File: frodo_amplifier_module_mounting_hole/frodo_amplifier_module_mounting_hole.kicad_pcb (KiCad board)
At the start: 2 copper layers, 16.5 x 24 mm, 24 parts, among them IC1 INA826AID, IC2 AS321KTR-G1, J1 Conn_01x01_Socket, J2 Conn_01x01_Socket, J3 Conn_01x01_Socket, J4 Conn_01x01_Socket, J5 Conn_01x01_Socket, J6 Conn_01x01_Socket, J7 Conn_01x01_Socket, J8 Conn_01x01_Socket

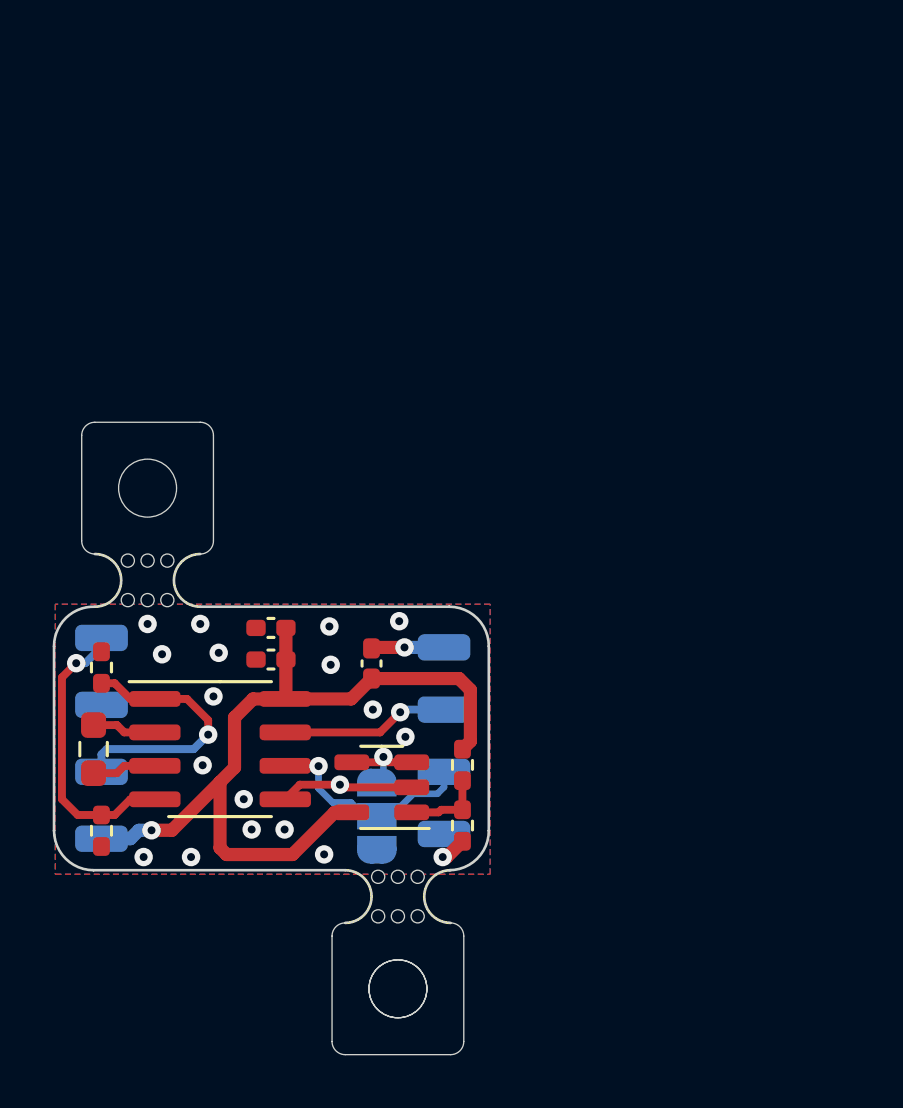
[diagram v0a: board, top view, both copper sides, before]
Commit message: updated mounting holes and footprints of c2 and fb1
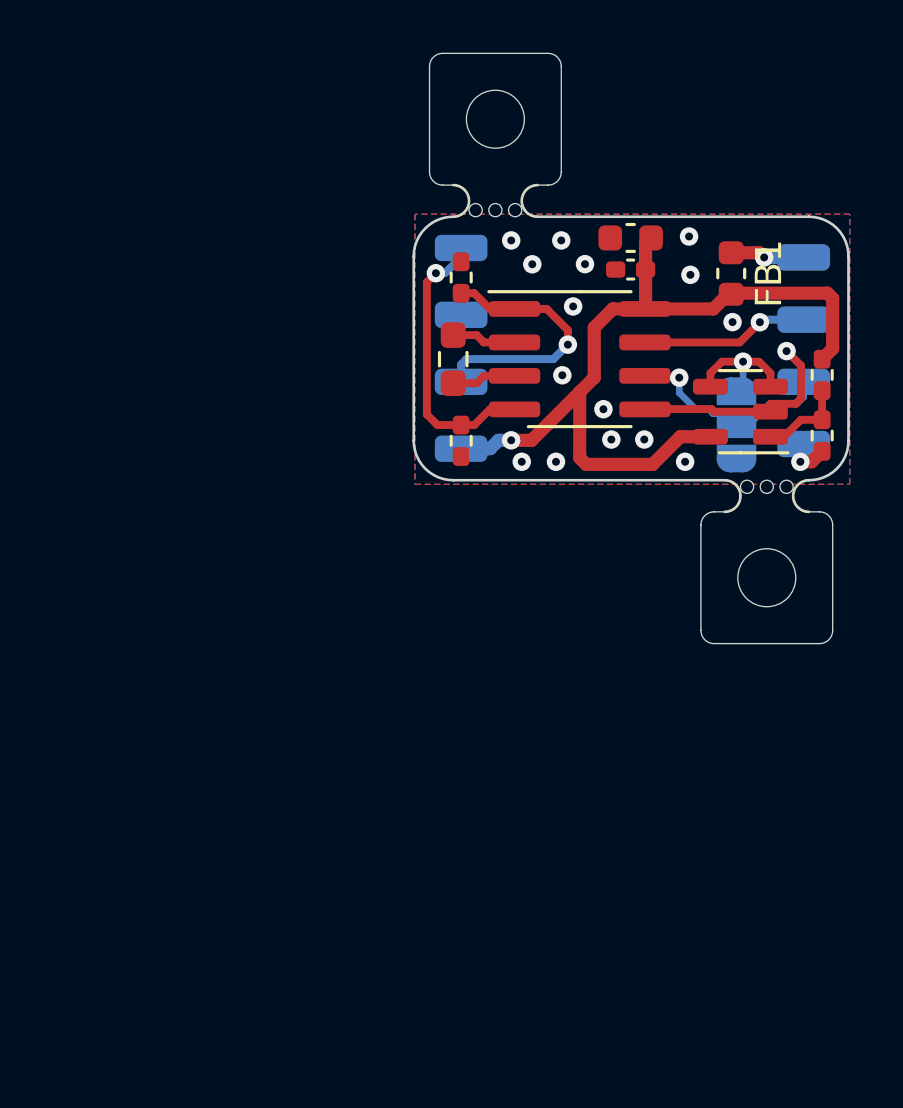
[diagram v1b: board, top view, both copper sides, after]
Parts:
- removed ?: , 
- C2: footprint Capacitor_SMD:C_0402_1005Metric_Pad0.74x0.62mm_HandSolder -> Capacitor_SMD:C_0603_1608Metric
- FB1: footprint Inductor_SMD:L_0402_1005Metric_Pad0.77x0.64mm_HandSolder -> Inductor_SMD:L_0603_1608Metric
- moved REF** 21.0 mm to (157.0, 82.9)
- moved mouse-bite-2mm-slot 20.4 mm to (157.0, 80.2)
- moved JP1 20.2 mm to (155.8, 77.1)
- moved C2 20.1 mm to (151.8, 70.0)
- moved J5 20.1 mm to (145.4, 78.0)
- moved R1 20.1 mm to (145.4, 71.5)
- moved R4 20.1 mm to (159.1, 77.5)
- moved C1 20.1 mm to (151.8, 71.2)
- moved FB1 20.1 mm to (155.7, 71.4)
- moved IC1 20.1 mm to (149.9, 74.6)
- moved J1 20.1 mm to (158.4, 70.7)
- moved J2 20.1 mm to (158.4, 73.1)
- moved J3 20.1 mm to (158.4, 75.5)
- moved J4 20.1 mm to (158.4, 77.8)
- moved J6 20.1 mm to (145.4, 70.4)
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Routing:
- net GND: track 6.07 -> 9.37 mm, vias 19 -> 17
- net Net-(IC2-INPUT_-): track 3.40 -> 4.99 mm
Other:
- board size 16.5 x 24 mm -> 16.5 x 22.4 mm
- board text added: "1-> gnd 3-> ref"
- board text removed: "1 for gnd 3 for ref"
